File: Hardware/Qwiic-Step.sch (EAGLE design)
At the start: 58 parts, among them J1 PTH, J2 Qwiic Right Angle, J3 5.5x2.1mm Barrel, J4 Qwiic Right Angle, J5 ISP, U1 A4988ALT1, U2 ATMEGA328P_TQFP, U4 HV7801, Y1 16MHz

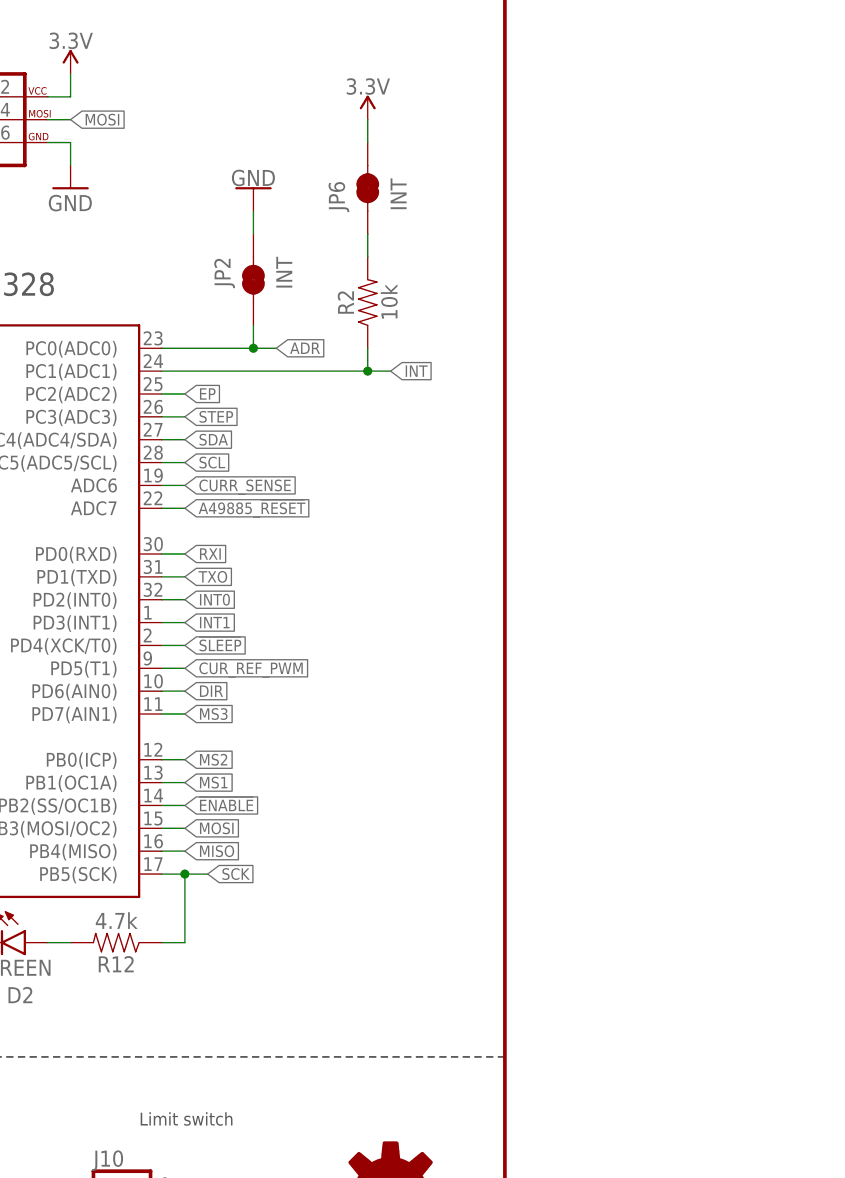
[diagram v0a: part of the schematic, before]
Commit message: Updated Qwiic Step board, working on examples for Rev 1 hardware
Updates to board:
Fixed serial programming pins
Moved ADR jumper to MOSI pin to free up GPIO
Moved A49885 reset pin to GPIO (from analog input pin)
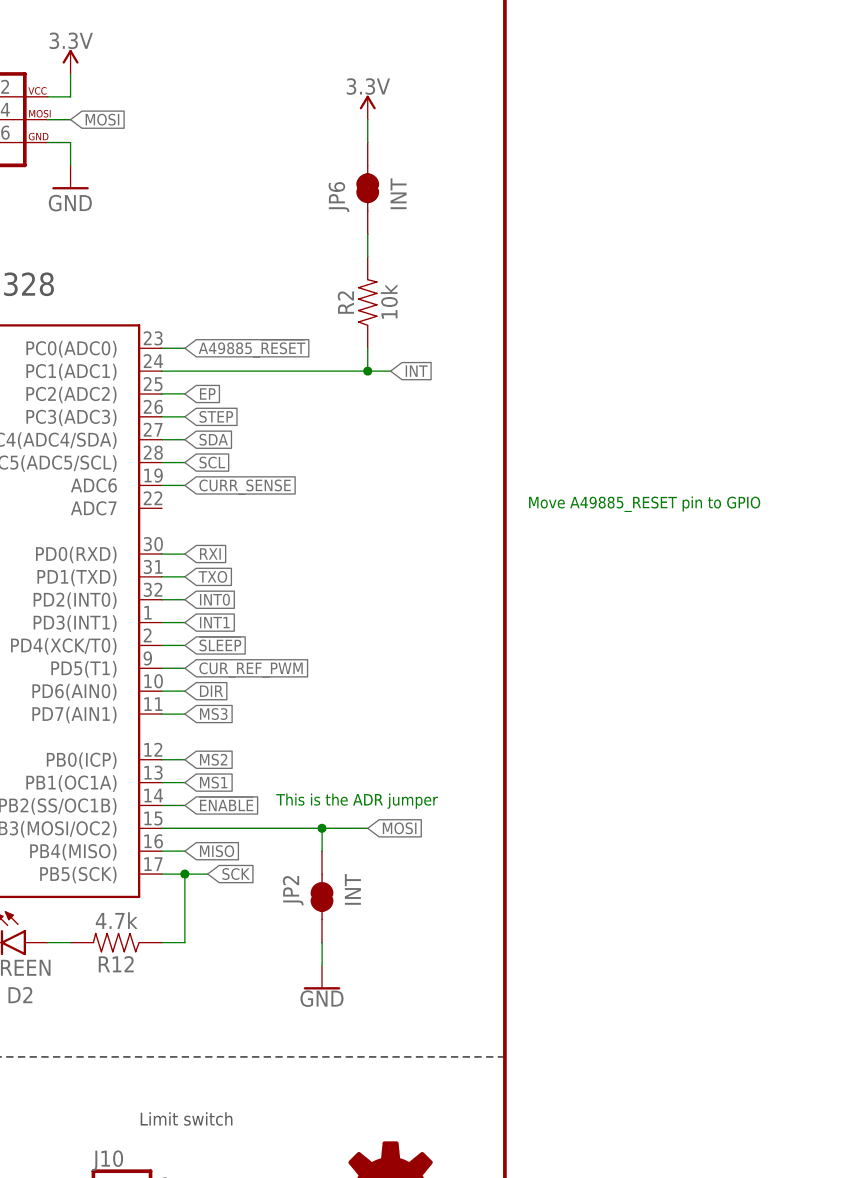
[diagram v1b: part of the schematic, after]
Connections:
- removed net ADR: JP2.2, U2.PC0(ADC0)
- net A49885_!RESET!: now also U2.PC0(ADC0); no longer U2.ADC7
- net GND: now also JP2.2; no longer JP2.1
- net MOSI: now also JP2.1
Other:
- note added: "Move A49885_RESET pin to GPIO"
- note added: "This is the ADR jumper"
- moved on the sheet: JP2
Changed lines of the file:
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@@
 <text x="2.54" y="20.32" size="1.4224" layer="97">3.5mm Screw Terminal</text>
 <text x="256.54" y="-2.54" size="1.27" layer="91">heat sink?</text>
+<text x="251.46" y="124.46" size="1.27" layer="91">Move A49885_RESET pin to GPIO</text>
+<text x="223.52" y="91.44" size="1.27" layer="91">This is the ADR jumper</text>
 </plain>
 <instances>
@@
 <attribute name="VALUE" x="147.32" y="160.274" size="1.778" layer="96" align="bottom-center"/>
 </instance>
-<instance part="GND20" gate="1" x="220.98" y="160.02" smashed="yes" rot="R180">
-<attribute name="VALUE" x="220.98" y="160.274" size="1.778" layer="96" rot="R180" align="top-center"/>
+<instance part="GND20" gate="1" x="228.6" y="71.12" smashed="yes">
+<attribute name="VALUE" x="228.6" y="70.866" size="1.778" layer="96" align="top-center"/>
 </instance>
 <instance part="SUPPLY23" gate="G$1" x="144.78" y="88.9" smashed="yes">
@@
 <attribute name="VALUE" x="54.864" y="84.201" size="1.778" layer="96" font="vector"/>
 </instance>
-<instance part="JP2" gate="G$1" x="220.98" y="149.86" smashed="yes" rot="MR270">
-<attribute name="NAME" x="218.44" y="152.4" size="1.778" layer="95" font="vector" rot="MR270"/>
-<attribute name="VALUE" x="223.52" y="152.4" size="1.778" layer="96" font="vector" rot="MR270" align="top-left"/>
+<instance part="JP2" gate="G$1" x="228.6" y="81.28" smashed="yes" rot="MR270">
+<attribute name="NAME" x="226.06" y="83.82" size="1.778" layer="95" font="vector" rot="MR270"/>
+<attribute name="VALUE" x="231.14" y="83.82" size="1.778" layer="96" font="vector" rot="MR270" align="top-left"/>
 </instance>
 <instance part="D5" gate="G$1" x="55.88" y="15.24" smashed="yes">
@@
 </segment>
 <segment>
-<pinref part="GND20" gate="1" pin="GND"/>
-<wire x1="220.98" y1="157.48" x2="220.98" y2="154.94" width="0.1524" layer="91"/>
-<pinref part="JP2" gate="G$1" pin="1"/>
-</segment>
-<segment>
 <pinref part="D4" gate="G$1" pin="C"/>
 <wire x1="134.62" y1="76.2" x2="134.62" y2="78.74" width="0.1524" layer="91"/>
@@
 <wire x1="-43.18" y1="129.54" x2="-43.18" y2="132.08" width="0.1524" layer="91"/>
 <wire x1="-43.18" y1="132.08" x2="-40.64" y2="132.08" width="0.1524" layer="91"/>
+</segment>
+<segment>
+<pinref part="GND20" gate="1" pin="GND"/>
+<pinref part="JP2" gate="G$1" pin="2"/>
+<wire x1="228.6" y1="73.66" x2="228.6" y2="76.2" width="0.1524" layer="91"/>
 </segment>
 </net>
@@
 </segment>
 </net>
-<net name="ADR" class="0">
-<segment>
-<wire x1="220.98" y1="142.24" x2="223.52" y2="142.24" width="0.1524" layer="91"/>
-<wire x1="220.98" y1="144.78" x2="220.98" y2="142.24" width="0.1524" layer="91"/>
-<label x="223.52" y="142.24" size="1.27" layer="95" rot="MR180" xref="yes"/>
-<pinref part="JP2" gate="G$1" pin="2"/>
-<pinref part="U2" gate="U1" pin="PC0(ADC0)"/>
-<wire x1="210.82" y1="142.24" x2="220.98" y2="142.24" width="0.1524" layer="91"/>
-<junction x="220.98" y="142.24"/>
-</segment>
-</net>
 <net name="N$26" class="0">
 <segment>
@@
 </segment>
 <segment>
-<pinref part="U2" gate="U1" pin="ADC7"/>
-<wire x1="210.82" y1="124.46" x2="213.36" y2="124.46" width="0.1524" layer="91"/>
-<label x="213.36" y="124.46" size="1.27" layer="95" xref="yes"/>
+<label x="213.36" y="142.24" size="1.27" layer="95" rot="MR180" xref="yes"/>
+<pinref part="U2" gate="U1" pin="PC0(ADC0)"/>
+<wire x1="210.82" y1="142.24" x2="213.36" y2="142.24" width="0.1524" layer="91"/>
 </segment>
 </net>
@@
 <segment>
 <pinref part="U2" gate="U1" pin="PB3(MOSI/OC2)"/>
-<wire x1="210.82" y1="88.9" x2="213.36" y2="88.9" width="0.1524" layer="91"/>
-<label x="213.36" y="88.9" size="1.27" layer="95" xref="yes"/>
-</segment>
-</net>
+<wire x1="210.82" y1="88.9" x2="228.6" y2="88.9" width="0.1524" layer="91"/>
+<label x="233.68" y="88.9" size="1.27" layer="95" xref="yes"/>
+<pinref part="JP2" gate="G$1" pin="1"/>
+<wire x1="228.6" y1="88.9" x2="233.68" y2="88.9" width="0.1524" layer="91"/>
+<wire x1="228.6" y1="86.36" x2="228.6" y2="88.9" width="0.1524" layer="91"/>
+<junction x="228.6" y="88.9"/>
+</segment>
+</net>

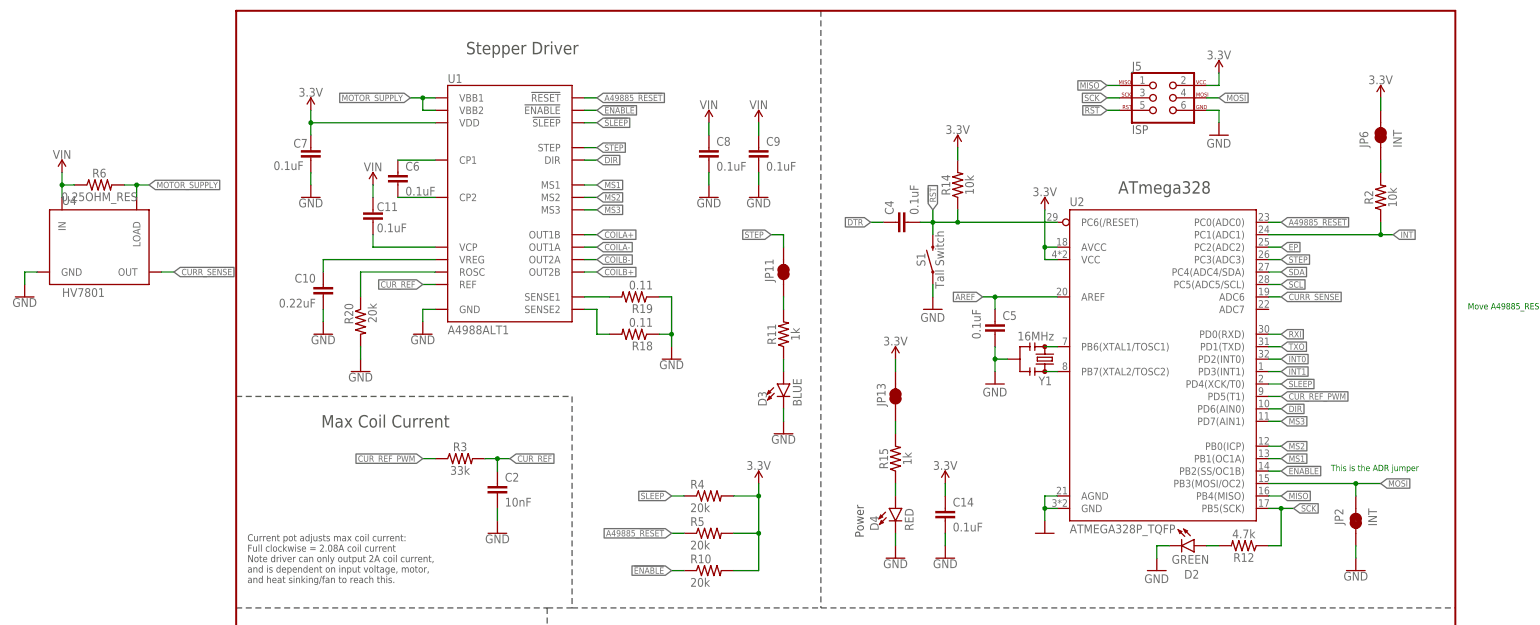
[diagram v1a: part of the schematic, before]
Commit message: Removed current sense IC. Switched around ADC pins
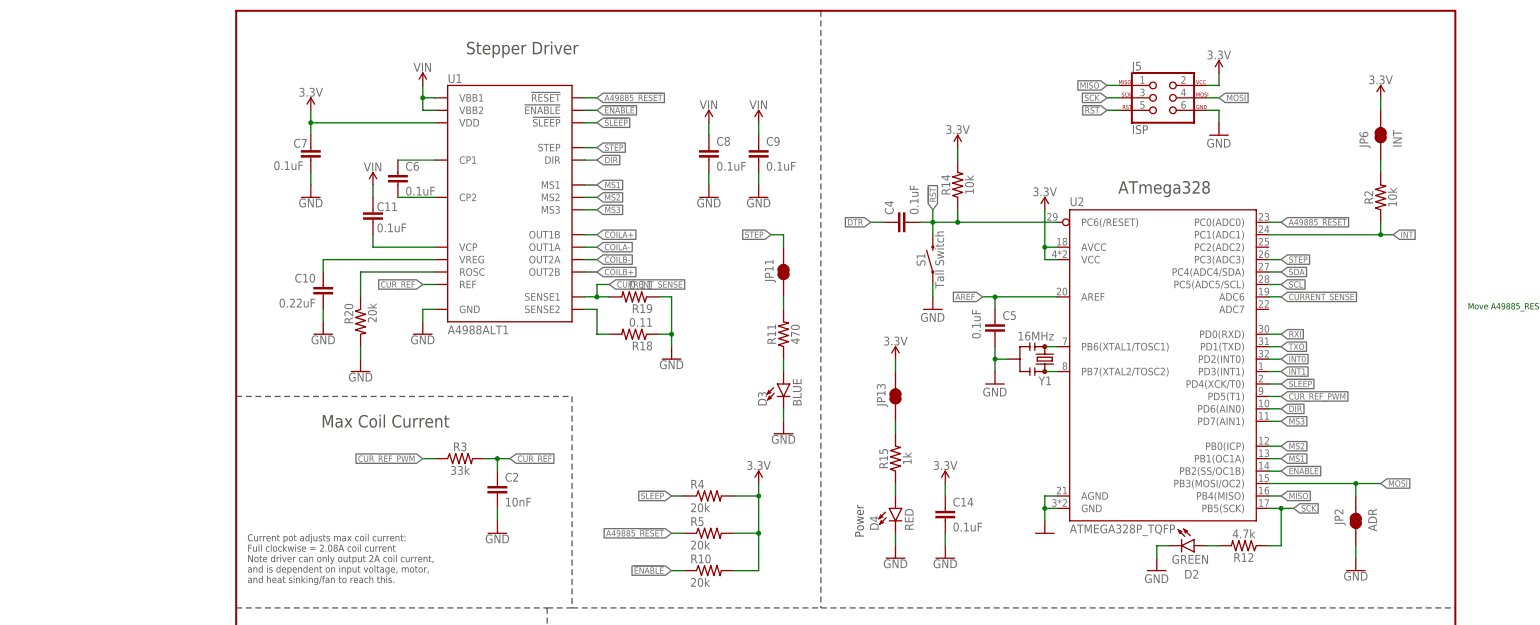
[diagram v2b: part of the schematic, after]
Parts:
- removed R6: 0.25OHM_RES, qwiic_step:0.25OHM_RES
- removed U4: HV7801, SparkFun-IC-Special-Function:HV7801
- JP2: value INT -> ADR
- R11: value 1k -> 470; device SparkFun-Resistors:1KOHM-0603-1/10W-1% -> SparkFun-Resistors:470OHM-0603-1/10W-1%
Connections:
- removed net CURR_SENSE: U2.ADC6, U4.OUT
- removed net EP: U2.PC2(ADC2)
- removed net MOTOR_SUPPLY: R6.2, U1.VBB1, U1.VBB2, U4.LOAD
- removed net N$32: R19.2, U1.SENSE1
- new net CURRENT_SENSE: R19.2, U1.SENSE1, U2.ADC6
- net GND: no longer U4.GND
- net VIN: now also U1.VBB1, U1.VBB2; no longer R6.1, U4.IN
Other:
- note removed: "This is the ADR jumper"
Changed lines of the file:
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@@
 <part name="JP10" library="SparkFun-Hardware" deviceset="STAND-OFF" device=""/>
 <part name="GND5" library="SparkFun-PowerSymbols" deviceset="GND" device=""/>
-<part name="R11" library="SparkFun-Resistors" deviceset="1KOHM" device="-0603-1/10W-1%" value="1k"/>
+<part name="R11" library="SparkFun-Resistors" deviceset="470OHM" device="-0603-1/10W-1%" value="470"/>
 <part name="D3" library="SparkFun-LED" deviceset="LED-BLUE" device="0603" value="BLUE"/>
 <part name="GND6" library="SparkFun-PowerSymbols" deviceset="GND" device=""/>
@@
 <part name="R3" library="SparkFun-Resistors" deviceset="33KOHM" device="-0603-1/10W-1%" value="33k"/>
 <part name="C2" library="SparkFun-Capacitors" deviceset="10NF" device="-0603-50V-10%" value="10nF"/>
-<part name="JP2" library="SparkFun-Jumpers" deviceset="JUMPER-SMT_2_NC_TRACE" device="_SILK" package3d_urn="urn:adsk.eagle:package:39281/1" value="INT"/>
+<part name="JP2" library="SparkFun-Jumpers" deviceset="JUMPER-SMT_2_NC_TRACE" device="_SILK" package3d_urn="urn:adsk.eagle:package:39281/1" value="ADR"/>
 <part name="D5" library="SparkFun-LED" deviceset="LED-YELLOW" device="0603" value="Yellow"/>
 <part name="J7" library="SparkFun-Connectors" deviceset="CONN_06" device="NO_SILK_NO_POP"/>
@@
 <part name="J11" library="SparkFun-Connectors" deviceset="CONN_01" device="PTH_NO_SILK_YES_STOP"/>
 <part name="SUPPLY10" library="SparkFun-PowerSymbols" deviceset="VIN" device=""/>
-<part name="GND23" library="SparkFun-PowerSymbols" deviceset="GND" device=""/>
 <part name="J9" library="SparkFun-Connectors" deviceset="CONN_02" device="LATCH_2"/>
 <part name="J6" library="SparkFun-Connectors" deviceset="CONN_04" device="LATCH"/>
-<part name="U4" library="SparkFun-IC-Special-Function" deviceset="HV7801" device=""/>
 <part name="SUPPLY2" library="SparkFun-PowerSymbols" deviceset="VIN" device=""/>
-<part name="R6" library="qwiic_step" deviceset="0.25OHM_RES" device=""/>
 </parts>
 <sheets>
@@
 <text x="256.54" y="-2.54" size="1.27" layer="91">heat sink?</text>
 <text x="251.46" y="124.46" size="1.27" layer="91">Move A49885_RESET pin to GPIO</text>
-<text x="223.52" y="91.44" size="1.27" layer="91">This is the ADR jumper</text>
 </plain>
 <instances>
@@
 <attribute name="NAME" x="124.46" y="13.208" size="1.778" layer="95" font="vector"/>
 </instance>
-<instance part="SUPPLY10" gate="G$1" x="-35.56" y="152.4" smashed="yes" rot="MR0">
-<attribute name="VALUE" x="-35.56" y="155.194" size="1.778" layer="96" rot="MR0" align="bottom-center"/>
-</instance>
-<instance part="GND23" gate="1" x="-43.18" y="127" smashed="yes" rot="MR0">
-<attribute name="VALUE" x="-43.18" y="126.746" size="1.778" layer="96" rot="MR0" align="top-center"/>
+<instance part="SUPPLY10" gate="G$1" x="38.1" y="170.18" smashed="yes" rot="MR0">
+<attribute name="VALUE" x="38.1" y="172.974" size="1.778" layer="96" rot="MR0" align="bottom-center"/>
 </instance>
 <instance part="J9" gate="G$1" x="7.62" y="10.16" smashed="yes">
@@
 <attribute name="NAME" x="96.52" y="18.288" size="1.778" layer="95" font="vector"/>
 </instance>
-<instance part="U4" gate="U1" x="-27.94" y="137.16" smashed="yes">
-<attribute name="NAME" x="-35.56" y="145.796" size="1.778" layer="95"/>
-<attribute name="VALUE" x="-35.56" y="127" size="1.778" layer="96"/>
-</instance>
 <instance part="SUPPLY2" gate="G$1" x="40.64" y="45.72" smashed="yes">
 <attribute name="VALUE" x="40.64" y="48.514" size="1.778" layer="96" align="bottom-center"/>
-</instance>
-<instance part="R6" gate="R1" x="-27.94" y="149.86" smashed="yes">
-<attribute name="NAME" x="-27.94" y="151.384" size="1.778" layer="95" font="vector" align="bottom-center"/>
-<attribute name="VALUE" x="-27.94" y="148.336" size="1.778" layer="96" font="vector" align="top-center"/>
 </instance>
 </instances>
@@
 </segment>
 <segment>
-<pinref part="GND23" gate="1" pin="GND"/>
-<pinref part="U4" gate="U1" pin="GND"/>
-<wire x1="-43.18" y1="129.54" x2="-43.18" y2="132.08" width="0.1524" layer="91"/>
-<wire x1="-43.18" y1="132.08" x2="-40.64" y2="132.08" width="0.1524" layer="91"/>
-</segment>
-<segment>
 <pinref part="GND20" gate="1" pin="GND"/>
 <pinref part="JP2" gate="G$1" pin="2"/>
@@
 </segment>
 </net>
-<net name="N$32" class="0">
-<segment>
-<wire x1="71.12" y1="127" x2="76.2" y2="127" width="0.1524" layer="91"/>
+<net name="CURRENT_SENSE" class="0">
+<segment>
+<wire x1="71.12" y1="127" x2="73.66" y2="127" width="0.1524" layer="91"/>
 <pinref part="R19" gate="G$1" pin="2"/>
 <pinref part="U1" gate="G$1" pin="SENSE1"/>
+<wire x1="73.66" y1="127" x2="76.2" y2="127" width="0.1524" layer="91"/>
+<wire x1="73.66" y1="127" x2="73.66" y2="129.54" width="0.1524" layer="91"/>
+<junction x="73.66" y="127"/>
+<wire x1="73.66" y1="129.54" x2="76.2" y2="129.54" width="0.1524" layer="91"/>
+<label x="76.2" y="129.54" size="1.27" layer="95" xref="yes"/>
+</segment>
+<segment>
+<pinref part="U2" gate="U1" pin="ADC6"/>
+<wire x1="210.82" y1="127" x2="213.36" y2="127" width="0.1524" layer="91"/>
+<label x="213.36" y="127" size="1.27" layer="95" xref="yes"/>
 </segment>
 </net>
@@
 </segment>
 <segment>
-<pinref part="U4" gate="U1" pin="IN"/>
-<wire x1="-35.56" y1="147.32" x2="-35.56" y2="149.86" width="0.1524" layer="91"/>
-<wire x1="-35.56" y1="149.86" x2="-33.02" y2="149.86" width="0.1524" layer="91"/>
+<wire x1="40.64" y1="165.1" x2="38.1" y2="165.1" width="0.1524" layer="91"/>
+<wire x1="38.1" y1="165.1" x2="38.1" y2="167.64" width="0.1524" layer="91"/>
+<wire x1="40.64" y1="167.64" x2="38.1" y2="167.64" width="0.1524" layer="91"/>
+<pinref part="U1" gate="G$1" pin="VBB1"/>
+<pinref part="U1" gate="G$1" pin="VBB2"/>
 <pinref part="SUPPLY10" gate="G$1" pin="VIN"/>
-<wire x1="-35.56" y1="149.86" x2="-35.56" y2="152.4" width="0.1524" layer="91"/>
-<junction x="-35.56" y="149.86"/>
-<pinref part="R6" gate="R1" pin="1"/>
+<wire x1="38.1" y1="170.18" x2="38.1" y2="167.64" width="0.1524" layer="91"/>
+<junction x="38.1" y="167.64"/>
 </segment>
 </net>
@@
 </segment>
 </net>
-<net name="EP" class="0">
-<segment>
-<pinref part="U2" gate="U1" pin="PC2(ADC2)"/>
-<wire x1="210.82" y1="137.16" x2="213.36" y2="137.16" width="0.1524" layer="91"/>
-<label x="213.36" y="137.16" size="1.27" layer="95" xref="yes"/>
-</segment>
-</net>
-<net name="CURR_SENSE" class="0">
-<segment>
-<pinref part="U2" gate="U1" pin="ADC6"/>
-<wire x1="210.82" y1="127" x2="213.36" y2="127" width="0.1524" layer="91"/>
-<label x="213.36" y="127" size="1.27" layer="95" xref="yes"/>
-</segment>
-<segment>
-<wire x1="-15.24" y1="132.08" x2="-12.7" y2="132.08" width="0.1524" layer="91"/>
-<label x="-12.7" y="132.08" size="1.27" layer="95" rot="MR180" xref="yes"/>
-<pinref part="U4" gate="U1" pin="OUT"/>
-</segment>
-</net>
-<net name="MOTOR_SUPPLY" class="2">
-<segment>
-<wire x1="40.64" y1="165.1" x2="38.1" y2="165.1" width="0.1524" layer="91"/>
-<wire x1="38.1" y1="165.1" x2="38.1" y2="167.64" width="0.1524" layer="91"/>
-<wire x1="40.64" y1="167.64" x2="38.1" y2="167.64" width="0.1524" layer="91"/>
-<pinref part="U1" gate="G$1" pin="VBB1"/>
-<pinref part="U1" gate="G$1" pin="VBB2"/>
-<wire x1="38.1" y1="167.64" x2="35.56" y2="167.64" width="0.1524" layer="91"/>
-<junction x="38.1" y="167.64"/>
-<label x="35.56" y="167.64" size="1.27" layer="95" rot="R180" xref="yes"/>
-</segment>
-<segment>
-<pinref part="U4" gate="U1" pin="LOAD"/>
-<wire x1="-20.32" y1="147.32" x2="-20.32" y2="149.86" width="0.1524" layer="91"/>
-<wire x1="-20.32" y1="149.86" x2="-22.86" y2="149.86" width="0.1524" layer="91"/>
-<wire x1="-20.32" y1="149.86" x2="-17.78" y2="149.86" width="0.1524" layer="91"/>
-<junction x="-20.32" y="149.86"/>
-<label x="-17.78" y="149.86" size="1.27" layer="95" xref="yes"/>
-<pinref part="R6" gate="R1" pin="2"/>
-</segment>
-</net>
